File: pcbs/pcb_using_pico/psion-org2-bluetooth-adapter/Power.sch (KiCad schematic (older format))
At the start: 28 parts, among them J3 Barrel_Jack, U5 BQ24072RGT, U6 AMS1117-3.3, U7 AMS1117-5.0

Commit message: Changed circuit to new power arrangement
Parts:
- removed C12, C13, C14: 100nF, Capacitor_SMD:C_0805_2012Metric, symbol Device:C_Small
- removed U6: AMS1117-3.3, Package_TO_SOT_SMD:SOT-223-3_TabPin2, symbol pak_breakout:AMS1117-3.3
- added C9: 100nF, Capacitor_SMD:C_0805_2012Metric, symbol Device:C_Small
- added D4: D_Schottky, Diode_SMD:D_SOD-123, symbol Device:D_Schottky
- U5: value BQ24072RGT -> BQ24079RGT
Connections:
- net labels removed: +3V3, +5V, VIN
- wire segments 93 -> 82
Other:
- note added: "12V* to 6V3\nDC\n*15V for some devices, 12V more \nconservative"
- note added: "5V"
- note added: "5V5 to VBAT"
- note removed: "XC9110C\n18650\nMCP73831\nMIC5504\n"
- moved on the sheet: BT1, C10, C11, C5, C6, C7, C8, D2, D3, J3, JP10, JP11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

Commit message: Added code
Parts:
- R7, R8: value R_Small -> 1k2
- R9: value R_Small -> 47k
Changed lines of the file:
@@
 P 4525 4925
 F 0 "R8" V 4329 4925 50  0000 C CNN
-F 1 "R_Small" V 4420 4925 50  0000 C CNN
+F 1 "1k2" V 4420 4925 50  0000 C CNN
 F 2 "Resistor_SMD:R_0805_2012Metric" H 4525 4925 50  0001 C CNN
 F 3 "~" H 4525 4925 50  0001 C CNN
@@
 P 4150 4825
 F 0 "R7" V 3954 4825 50  0000 C CNN
-F 1 "R_Small" V 4045 4825 50  0000 C CNN
+F 1 "1k2" V 4045 4825 50  0000 C CNN
 F 2 "Resistor_SMD:R_0805_2012Metric" H 4150 4825 50  0001 C CNN
 F 3 "~" H 4150 4825 50  0001 C CNN
@@
 P 4775 4425
 F 0 "R9" V 4579 4425 50  0000 C CNN
-F 1 "R_Small" V 4670 4425 50  0000 C CNN
+F 1 "47k" V 4670 4425 50  0000 C CNN
 F 2 "Resistor_SMD:R_0805_2012Metric" H 4775 4425 50  0001 C CNN
 F 3 "~" H 4775 4425 50  0001 C CNN

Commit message: Merged erroneous changes to V1.0 archive started
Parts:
- removed BT1: Battery_Cell, Battery:BatteryHolder_Keystone_1042_1x18650, symbol Device:Battery_Cell
- removed C10: 100nF, Capacitor_SMD:C_0805_2012Metric, symbol Device:C_Small
- removed C7: 4u7, Capacitor_SMD:C_1206_3216Metric_Pad1.42x1.75mm_HandSolder, symbol Device:C_Small
- removed C8: 10uF, Capacitor_SMD:C_1206_3216Metric_Pad1.42x1.75mm_HandSolder, symbol Device:C_Small
- removed D2, D3: LED, LED_SMD:LED_0805_2012Metric_Pad1.15x1.40mm_HandSolder, symbol Device:LED
- removed D4: D_Schottky, Diode_SMD:D_SOD-123, symbol Device:D_Schottky
- removed JP10, JP11, JP8, JP9: Jumper_NO_Small, Jumper:SolderJumper-2_P1.3mm_Open_RoundedPad1.0x1.5mm, symbol Device:Jumper_NO_Small
- removed R10: 10k, Resistor_SMD:R_0805_2012Metric, symbol Device:R_Small
- removed R11, R12: R_Small, Resistor_SMD:R_0805_2012Metric, symbol Device:R_Small
- removed R7, R8: 1k2, Resistor_SMD:R_0805_2012Metric, symbol Device:R_Small
- removed R9: 47k, Resistor_SMD:R_0805_2012Metric, symbol Device:R_Small
- removed U5: BQ24079RGT, Package_DFN_QFN:VQFN-16-1EP_3x3mm_P0.5mm_EP1.6x1.6mm, symbol Battery_Management:BQ24072RGT
- added BT2: Battery_Cell, Battery:BatteryHolder_Keystone_1042_1x18650, symbol Device:Battery_Cell
- added C12, C13, C14: 100nF, Capacitor_SMD:C_0805_2012Metric, symbol Device:C_Small
- added C15: 22uF, Capacitor_SMD:C_1206_3216Metric_Pad1.42x1.75mm_HandSolder, symbol Device:C_Small
- added C16: 10uF, Capacitor_SMD:C_1206_3216Metric_Pad1.42x1.75mm_HandSolder, symbol Device:C_Small
- added D4: LED, LED_SMD:LED_0805_2012Metric_Pad1.15x1.40mm_HandSolder, symbol Device:LED
- added DCDC1: dcdc, Connector_PinHeader_2.54mm:PinHeader_1x04_P2.54mm_Vertical, symbol New_Library:dcdc
- added J4: Connector_USB_B_Micro, Connector_USB:USB_Micro-B_GCT_USB3076-30-A, symbol cq1re1-cache:Connector_USB_B_Micro
- added L1: 2.2uH, Inductor_SMD:L_Coilcraft_LPS5030, symbol Device:L
- added R13: 2k2, Resistor_SMD:R_0805_2012Metric, symbol Device:R_Small
- added R14: 500R, Resistor_SMD:R_0805_2012Metric, symbol Device:R_Small
- added U6: AMS1117-3.3, Package_TO_SOT_SMD:SOT-223-3_TabPin2, symbol pak_breakout:AMS1117-3.3
- added U8: ETA6002, Package_SO:SOIC-8-1EP_3.9x4.9mm_P1.27mm_EP2.514x3.2mm, symbol pak_breakout:ETA6002
- C9: value 100nF -> 1uF; footprint Capacitor_SMD:C_0805_2012Metric -> Capacitor_SMD:C_1206_3216Metric_Pad1.42x1.75mm_HandSolder
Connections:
- net labels added: ESP_3V3
- wire segments 82 -> 78
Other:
- note added: "Battery voltage measurement\n"
- note added: "VREG can be powered from onboard battery or\nthe VBUS from the micro USB."
- note removed: "12V* to 6V3\nDC\n*15V for some devices, 12V more \nconservative"
- note removed: "5V"
- note removed: "5V5 to VBAT"
- moved on the sheet: C5, U7

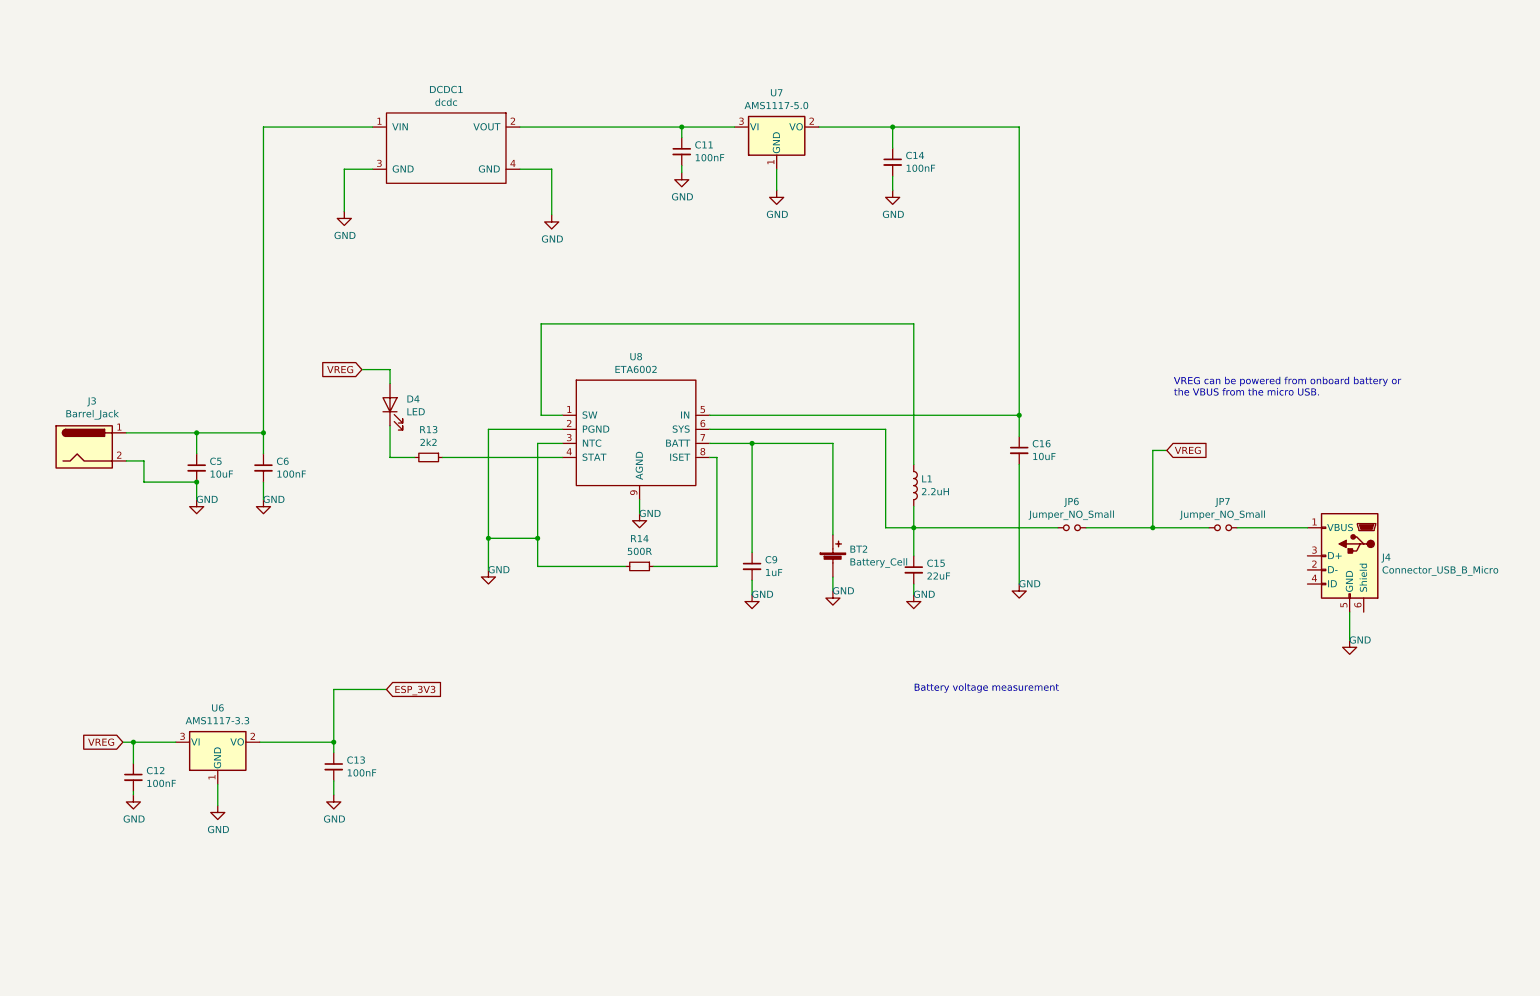
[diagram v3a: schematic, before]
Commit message: V2.0 sent off for fab. New charger IC with more solderable footprint, plus other fixes
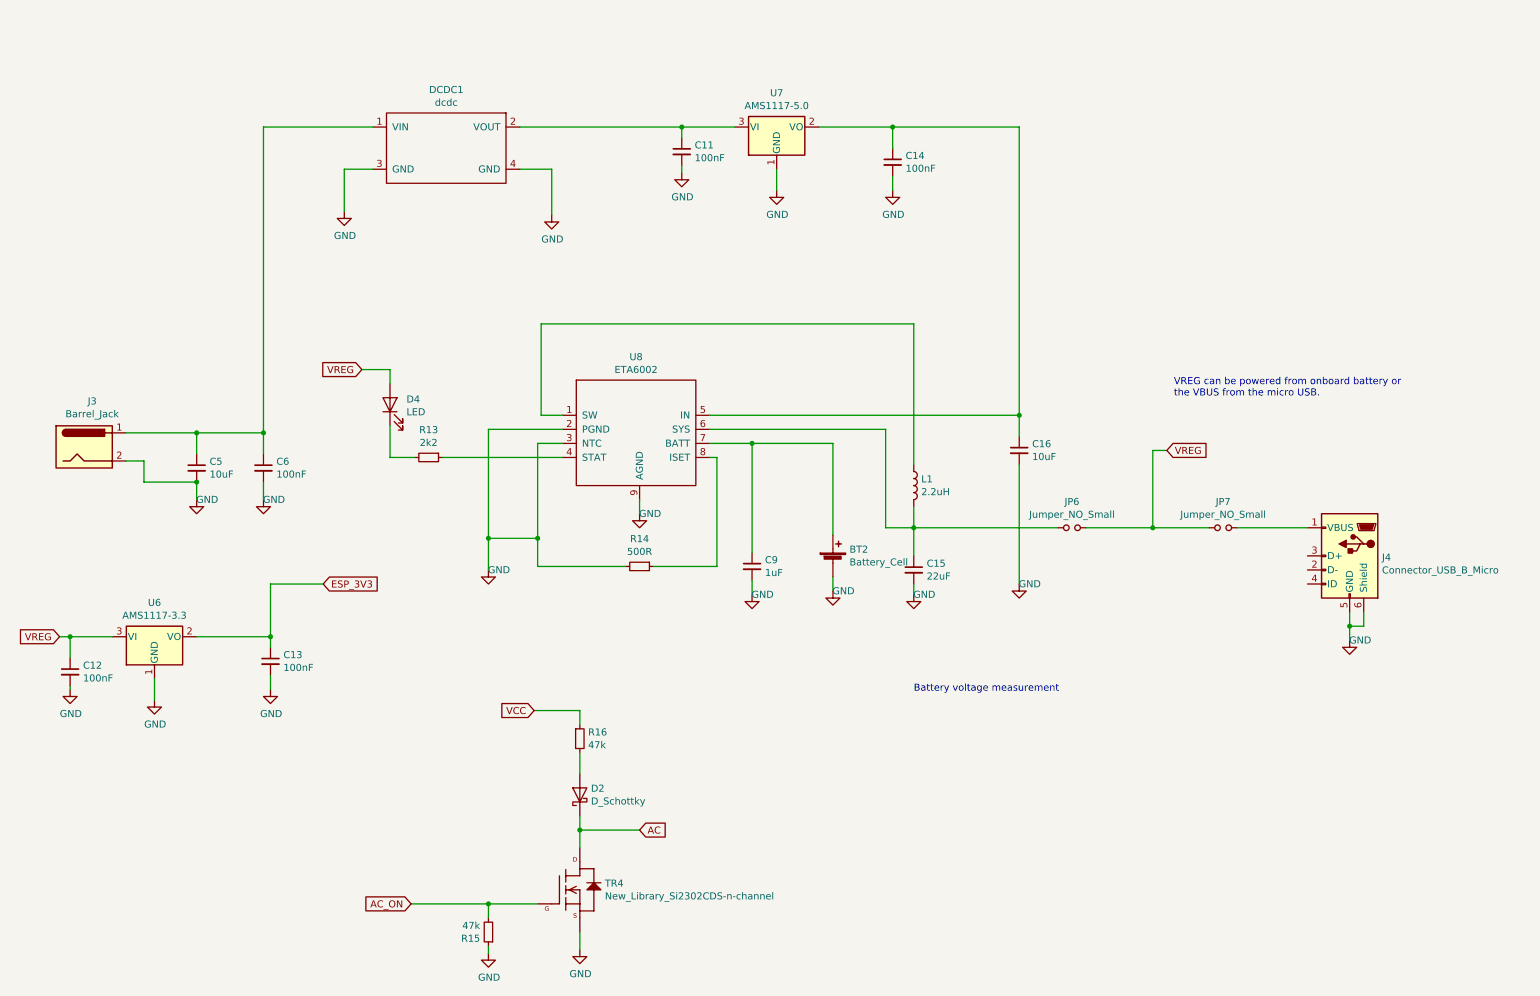
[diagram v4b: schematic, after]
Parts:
- added D2: D_Schottky, Diode_SMD:D_SOD-123, symbol Device:D_Schottky
- added R15, R16: 47k, Resistor_SMD:R_0805_2012Metric, symbol Device:R_Small
- added TR4: New_Library_Si2302CDS-n-channel, Package_TO_SOT_SMD:SOT-23, symbol cq1re1-cache:New_Library_Si2302CDS-n-channel
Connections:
- net GND: now also J4.6 (Shield), R15.1, TR4.2 (S)
- new net: D2.2 (A), R16.2
- new net AC: D2.1 (K), TR4.3 (D)
- new net AC_ON: R15.2, TR4.1 (G)
- new net VCC: R16.1
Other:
- moved on the sheet: C12, C13, U6
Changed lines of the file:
@@
 L pak_breakout:AMS1117-3.3 U6
 U 1 1 62080ABD
-P 2175 5925
-F 0 "U6" H 2175 6167 50  0000 C CNN
-F 1 "AMS1117-3.3" H 2175 6076 50  0000 C CNN
-F 2 "Package_TO_SOT_SMD:SOT-223-3_TabPin2" H 2175 6125 50  0001 C CNN
-F 3 "" H 2275 5675 50  0001 C CNN
-	1    2175 5925
+P 1725 5175
+F 0 "U6" H 1725 5417 50  0000 C CNN
+F 1 "AMS1117-3.3" H 1725 5326 50  0000 C CNN
+F 2 "Package_TO_SOT_SMD:SOT-223-3_TabPin2" H 1725 5375 50  0001 C CNN
+F 3 "" H 1825 4925 50  0001 C CNN
+	1    1725 5175
 	1    0    0    -1
 $EndComp
@@
 $EndComp
 Wire Wire Line
-	1875 5925 1575 5925
+	1425 5175 1125 5175
 Wire Wire Line
 	6975 1550 6450 1550
 Wire Wire Line
-	3000 5925 2475 5925
+	2550 5175 2025 5175
 $Comp
 L power:GND #PWR0124
 U 1 1 62080ABF
-P 2175 6375
-F 0 "#PWR0124" H 2175 6125 50  0001 C CNN
-F 1 "GND" H 2180 6202 50  0000 C CNN
-F 2 "" H 2175 6375 50  0001 C CNN
-F 3 "" H 2175 6375 50  0001 C CNN
-	1    2175 6375
+P 1725 5625
+F 0 "#PWR0124" H 1725 5375 50  0001 C CNN
+F 1 "GND" H 1730 5452 50  0000 C CNN
+F 2 "" H 1725 5625 50  0001 C CNN
+F 3 "" H 1725 5625 50  0001 C CNN
+	1    1725 5625
 	1    0    0    -1
 $EndComp
@@
 L power:GND #PWR0128
 U 1 1 61D244CA
-P 3000 6300
-F 0 "#PWR0128" H 3000 6050 50  0001 C CNN
-F 1 "GND" H 3005 6127 50  0000 C CNN
-F 2 "" H 3000 6300 50  0001 C CNN
-F 3 "" H 3000 6300 50  0001 C CNN
-	1    3000 6300
+P 2550 5550
+F 0 "#PWR0128" H 2550 5300 50  0001 C CNN
+F 1 "GND" H 2555 5377 50  0000 C CNN
+F 2 "" H 2550 5550 50  0001 C CNN
+F 3 "" H 2550 5550 50  0001 C CNN
+	1    2550 5550
 	1    0    0    -1
 $EndComp
@@
 L power:GND #PWR0130
 U 1 1 62080AC4
-P 1575 6300
-F 0 "#PWR0130" H 1575 6050 50  0001 C CNN
-F 1 "GND" H 1580 6127 50  0000 C CNN
-F 2 "" H 1575 6300 50  0001 C CNN
-F 3 "" H 1575 6300 50  0001 C CNN
-	1    1575 6300
+P 1125 5550
+F 0 "#PWR0130" H 1125 5300 50  0001 C CNN
+F 1 "GND" H 1130 5377 50  0000 C CNN
+F 2 "" H 1125 5550 50  0001 C CNN
+F 3 "" H 1125 5550 50  0001 C CNN
+	1    1125 5550
 	1    0    0    -1
 $EndComp
@@
 L Device:C_Small C12
 U 1 1 62080AC5
-P 1575 6175
-F 0 "C12" H 1667 6221 50  0000 L CNN
-F 1 "100nF" H 1667 6130 50  0000 L CNN
-F 2 "Capacitor_SMD:C_0805_2012Metric" H 1575 6175 50  0001 C CNN
-F 3 "~" H 1575 6175 50  0001 C CNN
-	1    1575 6175
+P 1125 5425
+F 0 "C12" H 1217 5471 50  0000 L CNN
+F 1 "100nF" H 1217 5380 50  0000 L CNN
+F 2 "Capacitor_SMD:C_0805_2012Metric" H 1125 5425 50  0001 C CNN
+F 3 "~" H 1125 5425 50  0001 C CNN
+	1    1125 5425
 	1    0    0    -1
 $EndComp
@@
 L Device:C_Small C13
 U 1 1 62080AC8
-P 3000 6100
-F 0 "C13" H 3092 6146 50  0000 L CNN
-F 1 "100nF" H 3092 6055 50  0000 L CNN
-F 2 "Capacitor_SMD:C_0805_2012Metric" H 3000 6100 50  0001 C CNN
-F 3 "~" H 3000 6100 50  0001 C CNN
-	1    3000 6100
+P 2550 5350
+F 0 "C13" H 2642 5396 50  0000 L CNN
+F 1 "100nF" H 2642 5305 50  0000 L CNN
+F 2 "Capacitor_SMD:C_0805_2012Metric" H 2550 5350 50  0001 C CNN
+F 3 "~" H 2550 5350 50  0001 C CNN
+	1    2550 5350
 	1    0    0    -1
 $EndComp
@@
 $EndComp
 Wire Wire Line
-	1575 6075 1575 5925
-Connection ~ 1575 5925
-Wire Wire Line
-	1575 5925 1500 5925
-Wire Wire Line
-	1575 6275 1575 6300
-Wire Wire Line
-	2175 6225 2175 6375
-Wire Wire Line
-	3000 5925 3000 6000
-Connection ~ 3000 5925
-Wire Wire Line
-	3000 6200 3000 6300
+	1125 5325 1125 5175
+Connection ~ 1125 5175
+Wire Wire Line
+	1125 5175 1050 5175
+Wire Wire Line
+	1125 5525 1125 5550
+Wire Wire Line
+	1725 5475 1725 5625
+Wire Wire Line
+	2550 5175 2550 5250
+Connection ~ 2550 5175
+Wire Wire Line
+	2550 5450 2550 5550
 Wire Wire Line
 	5475 1625 5475 1550
@@
 	2025 3725 2025 3875
 Connection ~ 2025 3725
-Text GLabel 1500 5925 0    50   Input ~ 0
+Text GLabel 1050 5175 0    50   Input ~ 0
 VREG
 $Comp
@@
 Text Notes 7125 5575 0    50   ~ 0
 Battery voltage measurement\n
-Text GLabel 3375 5550 2    50   Input ~ 0
+Text GLabel 2925 4800 2    50   Input ~ 0
 ESP_3V3
 Wire Wire Line
-	3375 5550 3000 5550
-Wire Wire Line
-	3000 5550 3000 5925
+	2925 4800 2550 4800
+Wire Wire Line
+	2550 4800 2550 5175
 $Comp
 L pak_breakout:ETA6002 U8
@@
 $EndComp
 Wire Wire Line
-	10225 5200 10225 5000
+	10225 5200 10225 5100
 $Comp
 L Device:Jumper_NO_Small JP6
@@
 Text Notes 8975 3475 0    50   ~ 0
 VREG can be powered from onboard battery or\nthe VBUS from the micro USB.
+Wire Wire Line
+	10325 5000 10325 5100
+Wire Wire Line
+	10325 5100 10225 5100
+Connection ~ 10225 5100
+Wire Wire Line
+	10225 5100 10225 5000
+$Comp
+L Device:R_Small R16
+U 1 1 6217ACB9
+P 4750 5900
+F 0 "R16" H 4809 5946 50  0000 L CNN
+F 1 "47k" H 4809 5855 50  0000 L CNN
+F 2 "Resistor_SMD:R_0805_2012Metric" H 4750 5900 50  0001 C CNN
+F 3 "~" H 4750 5900 50  0001 C CNN
+	1    4750 5900
+	1    0    0    -1
+$EndComp
+$Comp
+L Device:D_Schottky D2
+U 1 1 6217B564
+P 4750 6300
+F 0 "D2" V 4796 6221 50  0000 R CNN
+F 1 "D_Schottky" V 4705 6221 50  0000 R CNN
+F 2 "Diode_SMD:D_SOD-123" H 4750 6300 50  0001 C CNN
+F 3 "~" H 4750 6300 50  0001 C CNN
+	1    4750 6300
+	0    -1   -1   0
+$EndComp
+$Comp
+L cq1re1-cache:New_Library_Si2302CDS-n-channel TR4
+U 1 1 6217BC67
+P 4650 6975
+F 0 "TR4" H 4928 7021 50  0000 L CNN
+F 1 "New_Library_Si2302CDS-n-channel" H 4928 6930 50  0000 L CNN
+F 2 "Package_TO_SOT_SMD:SOT-23" H 4680 7125 20  0001 C CNN
+F 3 "" H 4650 6975 50  0001 C CNN
+	1    4650 6975
+	1    0    0    -1
+$EndComp
+$Comp
+L power:GND #PWR0140
+U 1 1 6217F360
+P 4750 7400
+F 0 "#PWR0140" H 4750 7150 50  0001 C CNN
+F 1 "GND" H 4755 7227 50  0000 C CNN
+F 2 "" H 4750 7400 50  0001 C CNN
+F 3 "" H 4750 7400 50  0001 C CNN
+	1    4750 7400
+	1    0    0    -1
+$EndComp
+Text GLabel 4425 5700 0    50   Input ~ 0
+VCC
+Wire Wire Line
+	4750 7400 4750 7275
+Wire Wire Line
+	4750 6675 4750 6550
+Wire Wire Line
+	4750 6150 4750 6000
+Wire Wire Line
+	4750 5800 4750 5700
+Wire Wire Line
+	4750 5700 4425 5700
+Text GLabel 3550 7075 0    50   Input ~ 0
+AC_ON
+$Comp
+L Device:R_Small R15
+U 1 1 6218AB59
+P 4100 7275
+F 0 "R15" H 4159 7321 50  0000 L CNN
+F 1 "47k" H 4159 7230 50  0000 L CNN
+F 2 "Resistor_SMD:R_0805_2012Metric" H 4100 7275 50  0001 C CNN
+F 3 "~" H 4100 7275 50  0001 C CNN
+	1    4100 7275
+	-1   0    0    1
+$EndComp
+$Comp
+L power:GND #PWR0141
+U 1 1 6218CCF5
+P 4100 7425
+F 0 "#PWR0141" H 4100 7175 50  0001 C CNN
+F 1 "GND" H 4105 7252 50  0000 C CNN
+F 2 "" H 4100 7425 50  0001 C CNN
+F 3 "" H 4100 7425 50  0001 C CNN
+	1    4100 7425
+	1    0    0    -1
+$EndComp
+Wire Wire Line
+	4100 7425 4100 7375
+Wire Wire Line
+	4450 7075 4100 7075
+Wire Wire Line
+	4100 7175 4100 7075
+Connection ~ 4100 7075
+Wire Wire Line
+	4100 7075 3550 7075
+Text GLabel 5175 6550 2    50   Input ~ 0
+AC
+Wire Wire Line
+	5175 6550 4750 6550
+Connection ~ 4750 6550
+Wire Wire Line
+	4750 6550 4750 6450
 $EndSCHEMATC

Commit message: Updates, psion link not working
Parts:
- U8: symbol pak_breakout:ETA6002 -> psion-org2-bluetooth-adapter-rescue:ETA6002-pak_breakout
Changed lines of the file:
@@
 	2550 4800 2550 5175
 $Comp
-L pak_breakout:ETA6002 U8
+L psion-org2-bluetooth-adapter-rescue:ETA6002-pak_breakout U8
 U 1 1 620E66C4
 P 4975 3500
